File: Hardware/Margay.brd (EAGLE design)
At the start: 50.2 x 30.4 mm, 73 parts, among them IC1 ATMEGA644M, J1 CONN_42.54_SCREW, J2 CONN_6SCREW_2.54, Q1 FDN360P, Q2 DMG3404, Q3 2N7002, Q4 FDN360P, U1 TPS7A0533DBV, U2 FT231X-Q

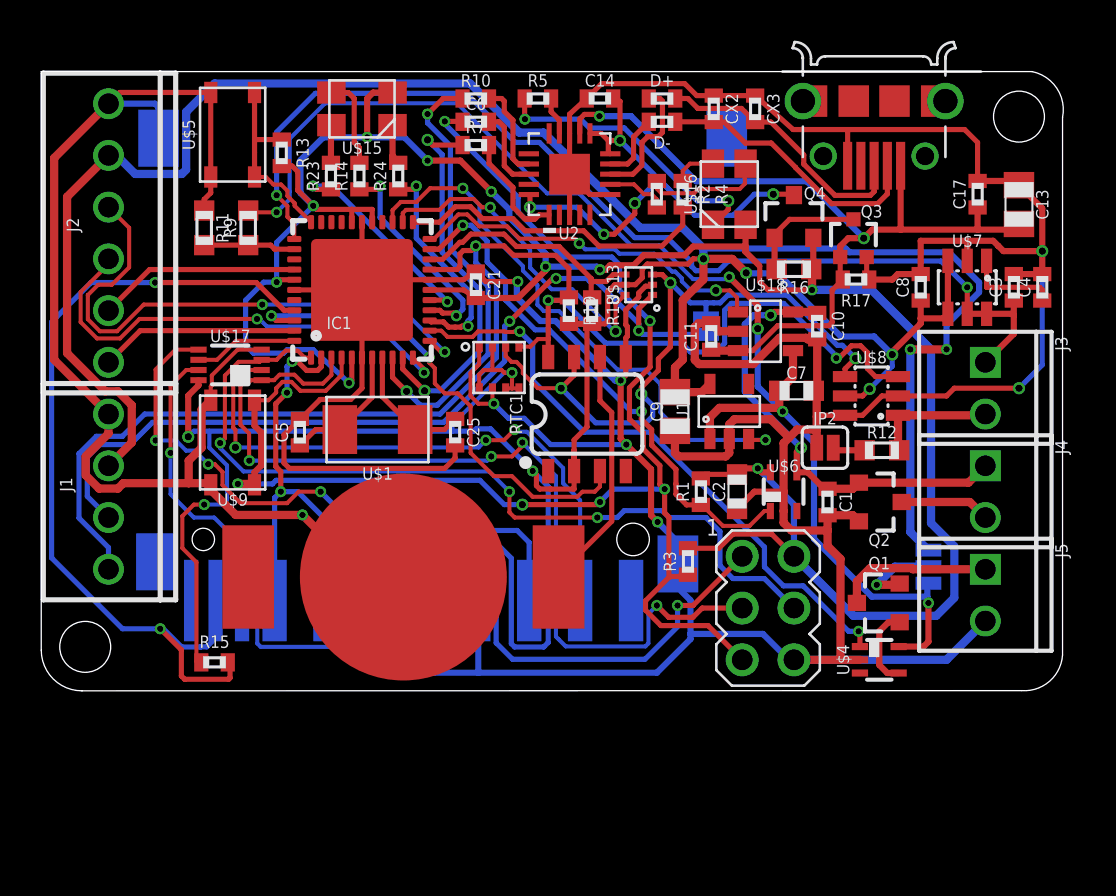
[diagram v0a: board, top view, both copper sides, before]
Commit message: Cleanup and silkscreen
Cleanup of traces, minor fix to overlap problem, relabeled silk screen to match new connections
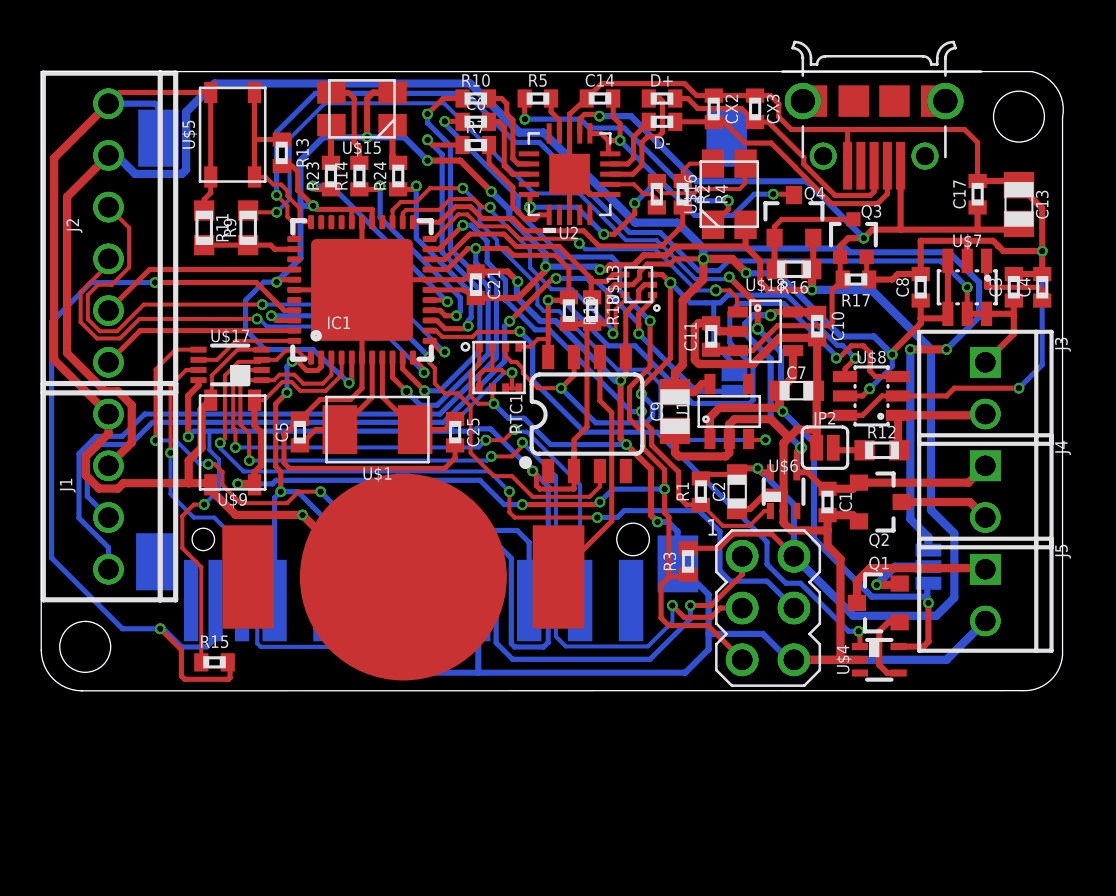
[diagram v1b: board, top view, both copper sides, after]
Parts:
- moved JP3 3.12 mm to (34.0, 15.1)
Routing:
- net SCL: track 72.5 -> 77.3 mm
- net SDA_OB: track 32.3 -> 35.5 mm
- net SDA_EXT: track 41.8 -> 44.6 mm
- net GND: track 305.6 -> 307.2 mm
- net RST: track 72.1 -> 71.2 mm
- net 3V3_AUX: track 203.5 -> 202.8 mm
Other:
- board text added: "A0"
- board text added: "D0"
- board text added: "RX"
- board text added: "TX"
- board text added: "±"
- board text removed: "CS"
- board text removed: "DI"
- board text removed: "DO"
- board text removed: "SCK"

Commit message: Condensed headers, added bat cap, added WDT
Condensed headers into 2 single piece headers, added capacitor on backup battery to deal with debouncing issue, also added WDT unit and replaced switched voltage output driver with unit switch instead of mosfet/comparator combo. Should double check/verify operation for WDT and integrated switch unit.
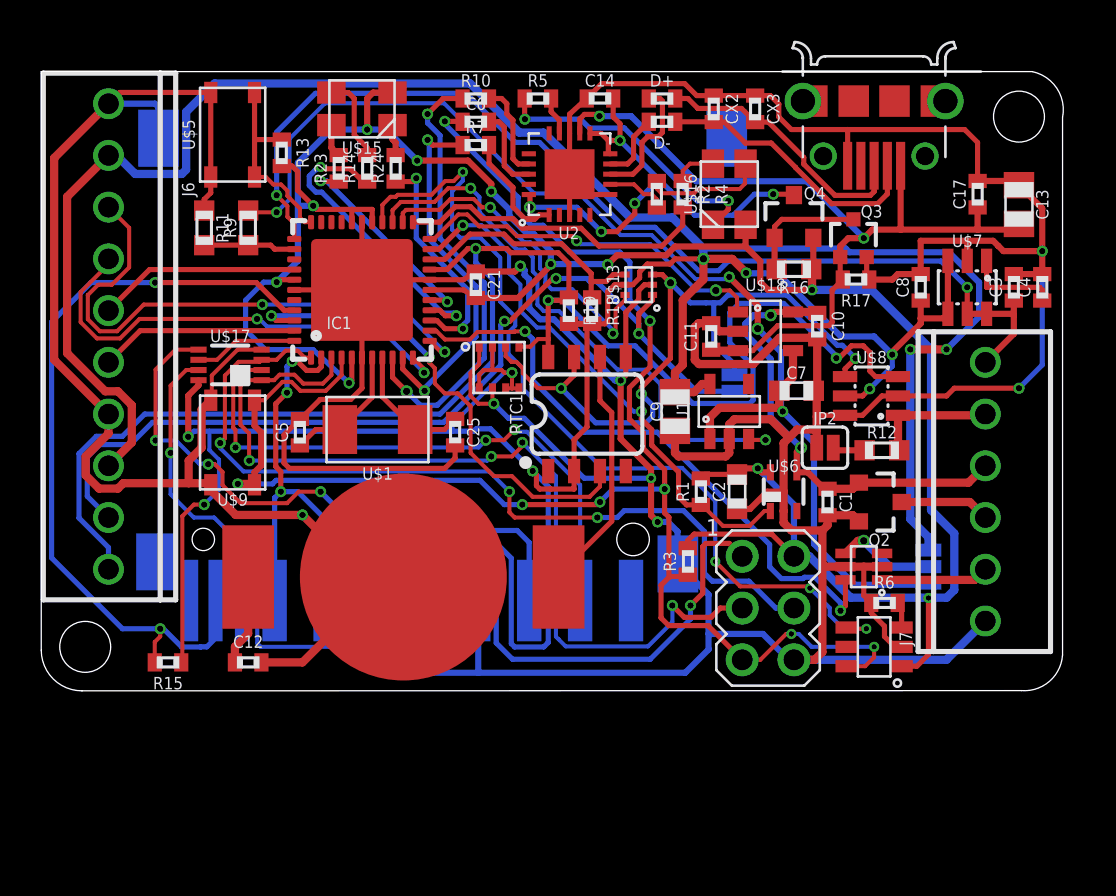
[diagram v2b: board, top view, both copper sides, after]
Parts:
- removed J1: CONN_42.54_SCREW, bschulz:1X04_SCREW
- removed J2: CONN_6SCREW_2.54, bschulz:1X06_SCREW
- removed J3, J4, J5: (no value), bschulz:1X02_2.54_SCREWTERM
- removed Q1: FDN360P, bschulz:SOT23-3
- removed U$4: MIC842H, bschulz:DCK_R-PDSO-G5
- added C12: 0.1uF, bschulz_passives:C0402
- added J6: (no value), bschulz:1X10_SCREW
- added J7: CONN_6SCREW_2.54, bschulz:1X06_SCREW
- added R6: 43k, bschulz_passives:R0402
- added U$10: MIC94090C6, bschulz:SC-70_6
- added U3: TPL5010DDC, bschulz:DDC_R-PDSO-G6
- moved R15 2.29 mm to (6.22, 1.40), turned to 0 degrees
- moved R23 0.54 mm to (14.6, 25.7)
- moved R14 0.54 mm to (16.0, 25.7)
- moved R24 0.40 mm to (17.4, 25.7)
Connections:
- new net WD_HOLD: IC1.26, U3.4
- net 3V3: now also U3.1
- net 3V3_AUX: now also J6.2, J6.8; no longer J1.3, J2.2
- net A0: now also J7.5; no longer J3.P1
- net ADC_EXT: now also J6.5; no longer J2.5
- net GND: now also C12.2, J6.1, J6.7, J7.1, R6.1, U$10.2, U$10.5, U2.EP, U3.2; no longer J1.4, J2.1, J5.P1, U$4.2, U2.21
- net GPIO_EXT: now also J6.6; no longer J2.6
- net N$2: now also R6.2, U3.3; no longer Q1.1, U$4.4
- net N$3: now also U$10.4; no longer Q1.2
- net N$31: now also C12.1
- net RST: now also U3.6
- net RX_EXT: now also J6.4; no longer J2.4
- net SCL: now also J6.10; no longer J1.1
- net SDA_EXT: now also J6.9; no longer J1.2
- net TX_EXT: now also J6.3; no longer J2.3
- net VBAT+: now also J7.4; no longer J4.P2
- net VBAT-: now also J7.3; no longer J4.P1
- net VBAT_SW: no longer U$4.5
- net VREF: now also J7.6; no longer J3.P2
- net VSWITCH: now also J7.2, U$10.1; no longer J5.P2, Q1.3
- net VSWITCH_CTRL: now also U$10.6; no longer U$4.1
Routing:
- net WD_HOLD: track 0.00 -> 43.3 mm, vias 0 -> 4
- net GND: track 307.2 -> 323.4 mm
- net RST: track 71.2 -> 80.8 mm, vias 6 -> 8
- net LED2: track 10.6 -> 15.1 mm
- net N$31: track 13.4 -> 17.9 mm
- net VBAT_SW: track 65.3 -> 61.0 mm, vias 5 -> 4
- net SD_CD: track 42.8 -> 38.5 mm
- net 3V3: track 114.1 -> 118.4 mm, vias 10 -> 11
- net N$2: track 3.95 -> 1.29 mm
- net VSWITCH: track 7.66 -> 5.29 mm
- net 3V3_AUX: track 202.8 -> 201.1 mm
- net MISO: track 54.6 -> 55.9 mm
- net N$3: track 4.19 -> 4.86 mm
- net 3V3_FTDI: track 24.8 -> 24.1 mm
- net TX: track 18.8 -> 18.2 mm

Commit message: Updated to new battery
Updated battery part to fix airwire issue
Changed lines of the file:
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@@
 <signal name="N$31">
 <contactref element="RTC1" pad="6"/>
-<contactref element="BT1" pad="POWER0"/>
-<contactref element="BT1" pad="POWER1"/>
+<contactref element="BT1" pad="POWER0" route="any" routetag="G$1.+"/>
+<contactref element="BT1" pad="POWER1" route="any" routetag="G$1.+"/>
 <wire x1="27.432" y1="14.24313125" x2="27.432" y2="16.389" width="0.254" layer="1"/>
 <wire x1="27.432" y1="14.24313125" x2="28.0114" y2="13.66373125" width="0.254" layer="1"/>
@@
 <wire x1="25.019" y1="5.334" x2="25.019" y2="5.08" width="0.254" layer="1"/>
 <wire x1="25.019" y1="5.08" x2="25.4" y2="5.588" width="0.254" layer="1"/>
-<wire x1="28.0114" y1="8.3264" x2="25.019" y2="5.334" width="0.254" layer="1"/>
 <contactref element="C12" pad="1"/>
 <wire x1="10.16" y1="5.588" x2="10.16" y2="2.809" width="0.4064" layer="1"/>
 <wire x1="10.16" y1="2.809" x2="9.51" y2="2.159" width="0.4064" layer="1"/>
 <wire x1="9.51" y1="2.159" x2="9.51" y2="1.397" width="0.4064" layer="1"/>
-<wire x1="10.16" y1="5.588" x2="25.019" y2="5.08" width="0" layer="19" extent="1-1"/>
+<wire x1="28.0114" y1="8.3264" x2="25.4" y2="5.715" width="0.254" layer="1"/>
+<wire x1="25.4" y1="5.715" x2="25.4" y2="5.588" width="0.254" layer="1"/>
 </signal>
 <signal name="RTC_INT">

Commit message: In progress of power switch upgrade
Midway through upgrade of power switch topology
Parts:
- added U$4: TPS22916YFP, bschulz:YFP0004
- added U4: TLV3691DPF, bschulz:DPF0006A
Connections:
- new net N$14: U$18.1, U4.4
- new net VMAIN: C7.1, JP1.3, U$18.4, U1.1
- net 3V3: now also U4.6
- net 3V3_FTDI: now also U4.3
- net GND: now also U$4.B1, U4.2
- net VBAT+: now also U$4.A2; no longer C10.1, U$18.5
- net VBAT_SW: now also C10.1, U$18.5, U$4.A1, U4.1; no longer C7.1, JP1.3, U$18.4, U1.1
- net VBAT_SW_CTRL: now also U$4.B2; no longer U$18.1
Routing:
- net VBAT_SW: track 61.0 -> 57.8 mm
- net VBAT+: track 22.5 -> 20.3 mm
- net VMAIN: track 0.00 -> 1.07 mm
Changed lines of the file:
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@@
 <attribute name="VALUE" x="50.546" y="2.159" size="0.6096" layer="27" font="vector" ratio="15" rot="R90"/>
 </element>
+<element name="U4" library="bschulz" package="DPF0006A" value="TLV3691DPF" x="2.54" y="-3.81" smashed="yes">
+<attribute name="DIGIKEY" value="296-37242-6-ND" x="2.54" y="-3.81" size="1.778" layer="27" display="off"/>
+<attribute name="MF" value="TI" x="2.54" y="-3.81" size="1.778" layer="27" display="off"/>
+<attribute name="MPN" value="TLV3691IDPFR" x="2.54" y="-3.81" size="1.778" layer="27" display="off"/>
+<attribute name="NAME" x="1.016" y="-3.81" size="0.6096" layer="25" font="vector" ratio="15" rot="R90" align="center"/>
+<attribute name="VALUE" x="4.064" y="-3.81" size="0.6096" layer="27" font="vector" ratio="15" rot="R90" align="center"/>
+</element>
+<element name="U$4" library="bschulz" package="YFP0004" value="TPS22916YFP" x="1.27" y="-7.62" smashed="yes"/>
 </elements>
 <signals>
@@
 <wire x1="43.561" y1="4.5593" x2="43.1927" y2="4.5593" width="0.254" layer="16"/>
 <wire x1="43.1927" y1="4.5593" x2="43.18" y2="4.572" width="0.254" layer="16"/>
+<contactref element="U4" pad="6"/>
+<wire x1="3.065" y1="-3.46" x2="11.001" y2="16.7556" width="0" layer="19" extent="1-16"/>
 </signal>
 <signal name="MOSI">
@@
 <wire x1="40.752" y1="4.318" x2="40.386" y2="4.684" width="0.254" layer="1"/>
 <wire x1="40.386" y1="4.684" x2="40.386" y2="6.096" width="0.254" layer="1"/>
+<contactref element="U4" pad="2"/>
+<contactref element="U$4" pad="B1"/>
+<wire x1="2.015" y1="-3.81" x2="10.81" y2="1.397" width="0" layer="19" extent="1-1"/>
+<wire x1="1.07" y1="-7.82" x2="2.015" y2="-3.81" width="0" layer="19" extent="1-1"/>
 </signal>
 <signal name="RST">
@@
 <wire x1="37.099" y1="11.7343" x2="37.3027" y2="11.938" width="0.3048" layer="1"/>
 <via x="37.3027" y="11.938" extent="1-16" drill="0.35"/>
-<contactref element="U$18" pad="5"/>
-<contactref element="C10" pad="1"/>
 <wire x1="40.148" y1="10.221" x2="39.848" y2="9.921" width="0.4064" layer="1"/>
 <wire x1="39.848" y1="9.921" x2="38.608" y2="9.921" width="0.4064" layer="1"/>
-<wire x1="38.1" y1="18.557" x2="38.054" y2="18.603" width="0.4064" layer="1"/>
-<wire x1="38.054" y1="18.603" x2="36.91" y2="18.603" width="0.4064" layer="1"/>
 <via x="35.814" y="18.4432" extent="1-16" drill="0.35"/>
 <wire x1="34.98405" y1="18.4432" x2="35.814" y2="18.4432" width="0.3048" layer="16"/>
 <wire x1="35.814" y1="18.4432" x2="35.9738" y2="18.603" width="0.3048" layer="1"/>
-<wire x1="35.9738" y1="18.603" x2="36.91" y2="18.603" width="0.3048" layer="1"/>
 <wire x1="37.3027" y1="11.938" x2="35.814" y2="13.4267" width="0.3048" layer="16"/>
 <wire x1="35.814" y1="16.28685" x2="34.5722" y2="17.52865" width="0.3048" layer="16"/>
@@
 <contactref element="J7" pad="4"/>
 <wire x1="46.355" y1="11.049" x2="45.527" y2="10.221" width="0.4064" layer="1"/>
+<contactref element="U$4" pad="A2"/>
+<wire x1="1.47" y1="-7.42" x2="37.099" y2="10.729" width="0" layer="19" extent="1-1"/>
 </signal>
 <signal name="VSWITCH_CTRL">
@@
 <wire x1="28.082" y1="28.179" x2="28.082" y2="29.083" width="0.254" layer="1"/>
 <wire x1="28.4178875" y1="27.8431125" x2="28.082" y2="28.179" width="0.254" layer="1"/>
+<contactref element="U4" pad="3"/>
+<wire x1="30.5133875" y1="24.9253875" x2="30.893546875" y2="24.545228125" width="0" layer="19" extent="16-16"/>
+<wire x1="2.015" y1="-4.16" x2="23.9974" y2="23.7434" width="0" layer="19" extent="1-1"/>
 </signal>
 <signal name="VBAT_SW">
-<contactref element="C7" pad="1"/>
 <contactref element="R9" pad="2"/>
-<contactref element="JP1" pad="3"/>
 <via x="33.782" y="20.32" extent="1-16" drill="0.3"/>
 <via x="11.557" y="23.495" extent="1-16" drill="0.3"/>
@@
 <wire x1="28.4495625" y1="22.37899375" x2="29.96705" y2="22.37899375" width="0.2" layer="16"/>
 <via x="36.4056" y="13.716" extent="1-16" drill="0.3"/>
-<wire x1="43.561" y1="5.2832" x2="43.5054" y2="5.2276" width="0.3048" layer="16"/>
 <wire x1="37.942603125" y1="12.178996875" x2="37.942603125" y2="7.208603125" width="0.3048" layer="16"/>
 <wire x1="37.942603125" y1="12.178996875" x2="36.4056" y2="13.716" width="0.3048" layer="16"/>
-<contactref element="U$18" pad="4"/>
-<contactref element="U1" pad="1"/>
-<wire x1="36.234" y1="14.732" x2="36.91" y2="15.408" width="0.4064" layer="1"/>
-<wire x1="36.91" y1="15.408" x2="36.91" y2="16.703" width="0.4064" layer="1"/>
 <wire x1="36.4056" y1="13.716" x2="36.234" y2="13.8876" width="0.4064" layer="1"/>
-<wire x1="36.234" y1="13.8876" x2="36.234" y2="14.732" width="0.4064" layer="1"/>
 <wire x1="36.2278" y1="13.8938" x2="33.29653125" y2="13.8938" width="0.4064" layer="1"/>
 <wire x1="36.2278" y1="13.8938" x2="36.4056" y2="13.716" width="0.4064" layer="1"/>
 <wire x1="33.29653125" y1="13.8938" x2="32.832" y2="13.42926875" width="0.4064" layer="1"/>
-<wire x1="32.832" y1="13.42926875" x2="32.832" y2="12.366" width="0.4064" layer="1"/>
 <wire x1="36.4056" y1="13.716" x2="36.322" y2="13.7996" width="0.3048" layer="16"/>
 <wire x1="36.322" y1="13.7996" x2="36.322" y2="16.637" width="0.3048" layer="16"/>
@@
 <wire x1="12.1964" y1="24.1344" x2="11.557" y2="23.495" width="0.2" layer="16"/>
 <wire x1="36.322" y1="16.637" x2="35.179" y2="17.78" width="0.3048" layer="16"/>
-<wire x1="43.538" y1="5.2602" x2="43.561" y2="5.2832" width="0.3048" layer="16"/>
 <wire x1="37.942603125" y1="7.208603125" x2="39.94420625" y2="5.207" width="0.3048" layer="16"/>
-<wire x1="43.561" y1="5.207" x2="43.561" y2="5.2832" width="0.3048" layer="16"/>
 <wire x1="39.94420625" y1="5.207" x2="43.561" y2="5.207" width="0.3048" layer="16"/>
+<contactref element="U$4" pad="A1"/>
+<contactref element="U4" pad="1"/>
+<contactref element="U$18" pad="5"/>
+<contactref element="C10" pad="1"/>
+<wire x1="38.1" y1="18.557" x2="38.054" y2="18.603" width="0.4064" layer="1"/>
+<wire x1="38.054" y1="18.603" x2="36.91" y2="18.603" width="0.4064" layer="1"/>
+<wire x1="35.179" y1="18.923" x2="36.91" y2="18.603" width="0" layer="19" extent="1-1"/>
+<wire x1="2.015" y1="-3.46" x2="10.248" y2="23.495" width="0" layer="19" extent="1-1"/>
+<wire x1="1.07" y1="-7.42" x2="2.015" y2="-3.46" width="0" layer="19" extent="1-1"/>
 </signal>
 <signal name="3V3_AUX">
@@
 <via x="26.289" y="22.098" extent="1-16" drill="0.3"/>
 <wire x1="26.289" y1="22.098" x2="26.4557" y2="21.9313" width="0.2" layer="16"/>
-<contactref element="U$18" pad="1"/>
 <wire x1="26.4557" y1="21.9313" x2="29.90674375" y2="21.9313" width="0.2" layer="16"/>
 <wire x1="32.17824375" y1="19.6598" x2="33.1218375" y2="19.6598" width="0.2" layer="16"/>
@@
 <wire x1="33.8072" y1="19.6598" x2="34.163" y2="19.304" width="0.2" layer="1"/>
 <wire x1="34.163" y1="19.304" x2="34.163" y2="18.65" width="0.2" layer="1"/>
-<wire x1="34.163" y1="18.65" x2="34.21" y2="18.603" width="0.2" layer="1"/>
+<contactref element="U$4" pad="B2"/>
+<wire x1="1.47" y1="-7.82" x2="19.073" y2="22.185" width="0" layer="19" extent="1-1"/>
 </signal>
 <signal name="SDA_EXT">
@@
 <wire x1="42.244" y1="4.126" x2="42.052" y2="4.318" width="0.254" layer="1"/>
 </signal>
+<signal name="VMAIN">
+<contactref element="U$18" pad="4"/>
+<contactref element="JP1" pad="3"/>
+<wire x1="43.561" y1="5.2832" x2="43.5054" y2="5.2276" width="0.3048" layer="16"/>
+<wire x1="43.538" y1="5.2602" x2="43.561" y2="5.2832" width="0.3048" layer="16"/>
+<contactref element="C7" pad="1"/>
+<contactref element="U1" pad="1"/>
+<wire x1="36.234" y1="14.732" x2="36.91" y2="15.408" width="0.4064" layer="1"/>
+<wire x1="36.91" y1="15.408" x2="36.91" y2="16.703" width="0" layer="19" extent="1-1"/>
+<wire x1="32.832" y1="12.366" x2="36.234" y2="14.732" width="0" layer="19" extent="1-1"/>
+<wire x1="43.561" y1="5.2832" x2="36.234" y2="14.732" width="0" layer="19" extent="1-16"/>
+</signal>
+<signal name="N$14">
+<contactref element="U4" pad="4"/>
+<contactref element="U$18" pad="1"/>
+<wire x1="3.065" y1="-4.16" x2="34.21" y2="18.603" width="0" layer="19" extent="1-1"/>
+</signal>
 </signals>
